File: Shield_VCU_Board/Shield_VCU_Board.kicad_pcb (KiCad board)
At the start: 2 copper layers, 250.5 x 107.1 mm, 156 parts, among them J1 Conn_02x08_Odd_Even, J10 Main_Supply, J11 Conn_01x40_Socket, J13 Conn_Molex_TouchPanel, J14 CAN_OUT, J15 Conn_01x04_Socket, J2 Conn_02x10_Odd_Even, J3/1 NXP3, J4 Conn_02x08_Odd_Even, J5 Conn_02x10_Odd_Even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

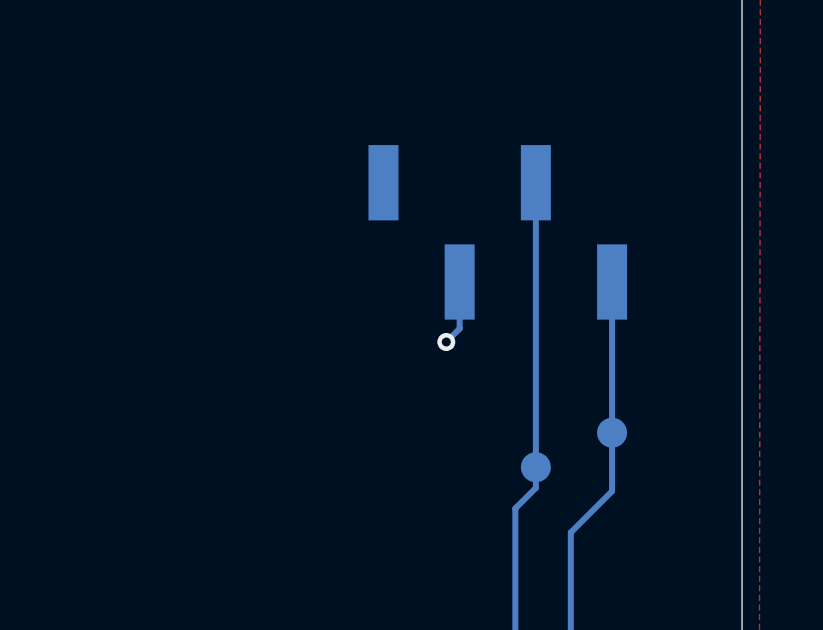
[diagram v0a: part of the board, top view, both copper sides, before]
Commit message: CAN GND removed
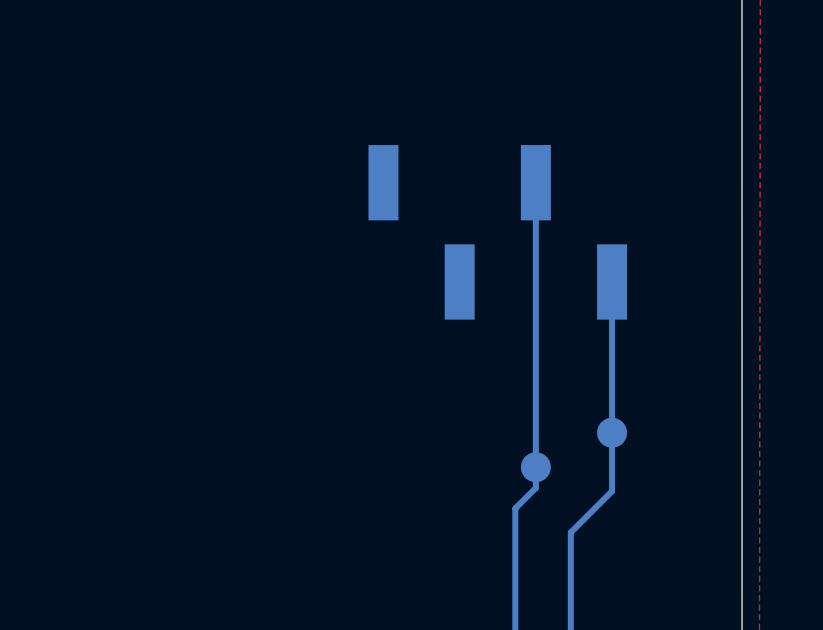
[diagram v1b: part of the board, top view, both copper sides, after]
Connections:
- J15 pad 3: GND -> unconnected-(J15-Pin_3-Pad3)
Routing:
- net GND: track 794.6 -> 792.4 mm, vias 47 -> 46
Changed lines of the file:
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@@
 	(net 253 "Net-(Q4-E)")
 	(net 254 "Net-(Q4-B)")
+	(net 255 "unconnected-(J15-Pin_3-Pad3)")
 	(footprint "MountingHole:MountingHole_2.7mm_M2.5_Pad"
 		(locked yes)
@@
 			(size 2.51 1)
 			(layers "B.Cu" "B.Mask" "B.Paste")
-			(net 35 "GND")
+			(net 255 "unconnected-(J15-Pin_3-Pad3)")
 			(pinfunction "Pin_3")
-			(pintype "passive")
+			(pintype "passive+no_connect")
 		)
 		(pad "4" smd rect
@@
 	)
 	(via
-		(at 265.65 114.65)
-		(size 0.6)
-		(drill 0.3)
-		(layers "F.Cu" "B.Cu")
-		(net 35)
-	)
-	(via
 		(at 178.39 101.98)
 		(size 0.6)
@@
 	)
 	(segment
-		(start 265.65 114.65)
-		(end 266.095 114.205)
-		(width 0.2)
-		(layer "B.Cu")
-		(net 35)
-	)
-	(segment
 		(start 131.7973 75.555878)
 		(end 133.155878 75.555878)
@@
 		(width 0.2)
 		(layer "B.Cu")
-		(net 35)
-	)
-	(segment
-		(start 266.095 114.205)
-		(end 266.095 112.65)
-		(width 0.2)
-		(layer "B.Cu")

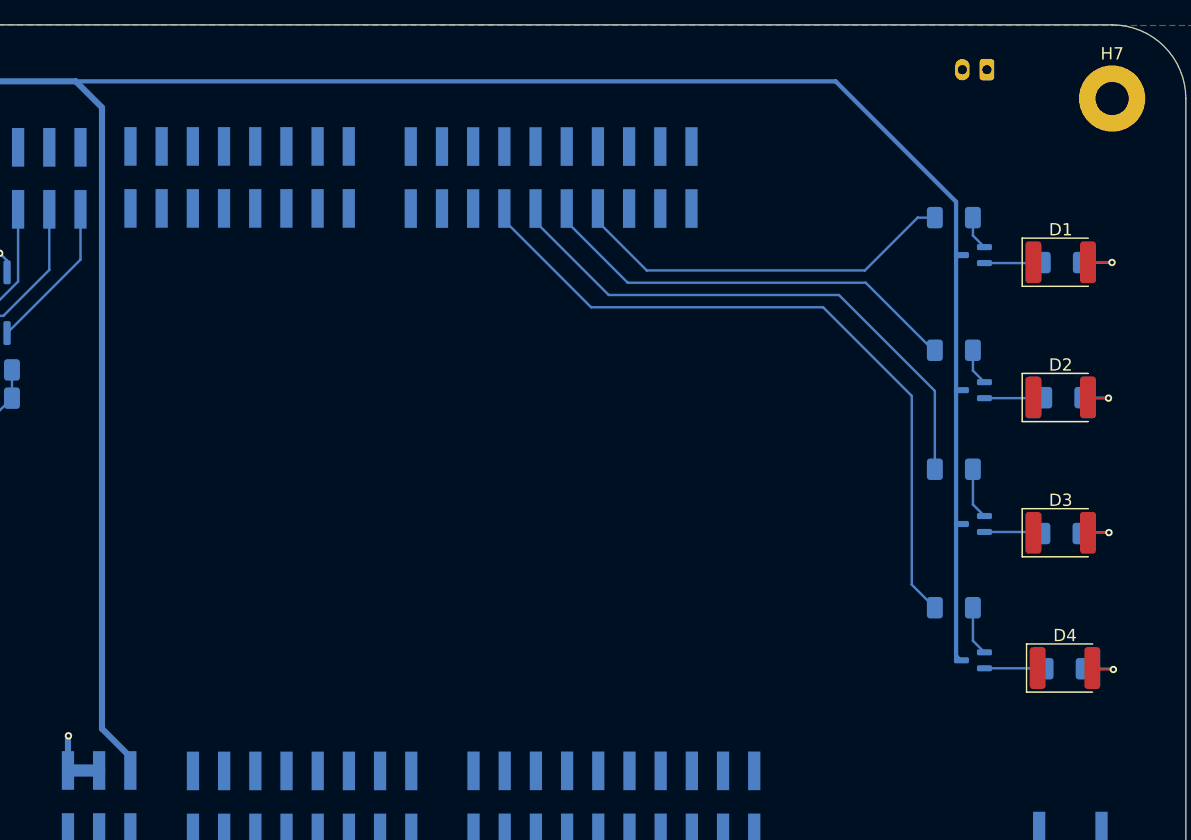
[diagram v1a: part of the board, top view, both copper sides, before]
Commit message: BJT to MOS transfer + new LED
NMOS Datasheet: https://www.onsemi.com/pdf/datasheet/bss138-d.pdf

LED Datasheet:    https://www.mouser.com/catalog/specsheets/ams%20OSRAM_04-30-2025_LS%20ETSF.01_EN.pdf?_gl=1*1llmkcu*_gcl_aw*R0NMLjE3NzI3MDEzNDUuQ2owS0NRandyczJYQmhEakFSSXNBSFZ5bW1UcjlpUWl6aF9Xd1RWYXh4LTl0ajlzSlFKZG9HR05zd3FjQVM0alhPYTRFS0o3bm1nUzBiZ2FBcThfRUFMd193Y0I.*_gcl_au*MTE2NzkxNzkuMTc3MjcwMTMwNy4xMzk2Njg4ODk2LjE3NzQzNTc3NjAuMTc3NDM1Nzc2NA..*_ga*NjEyNjEzMjQ1LjE3NzI3MDEzMDc.*_ga_15W4STQT4T*czE3NzQzNTMzOTckbzE2JGcxJHQxNzc0MzU4MTE2JGoyOCRsMCRoMA..
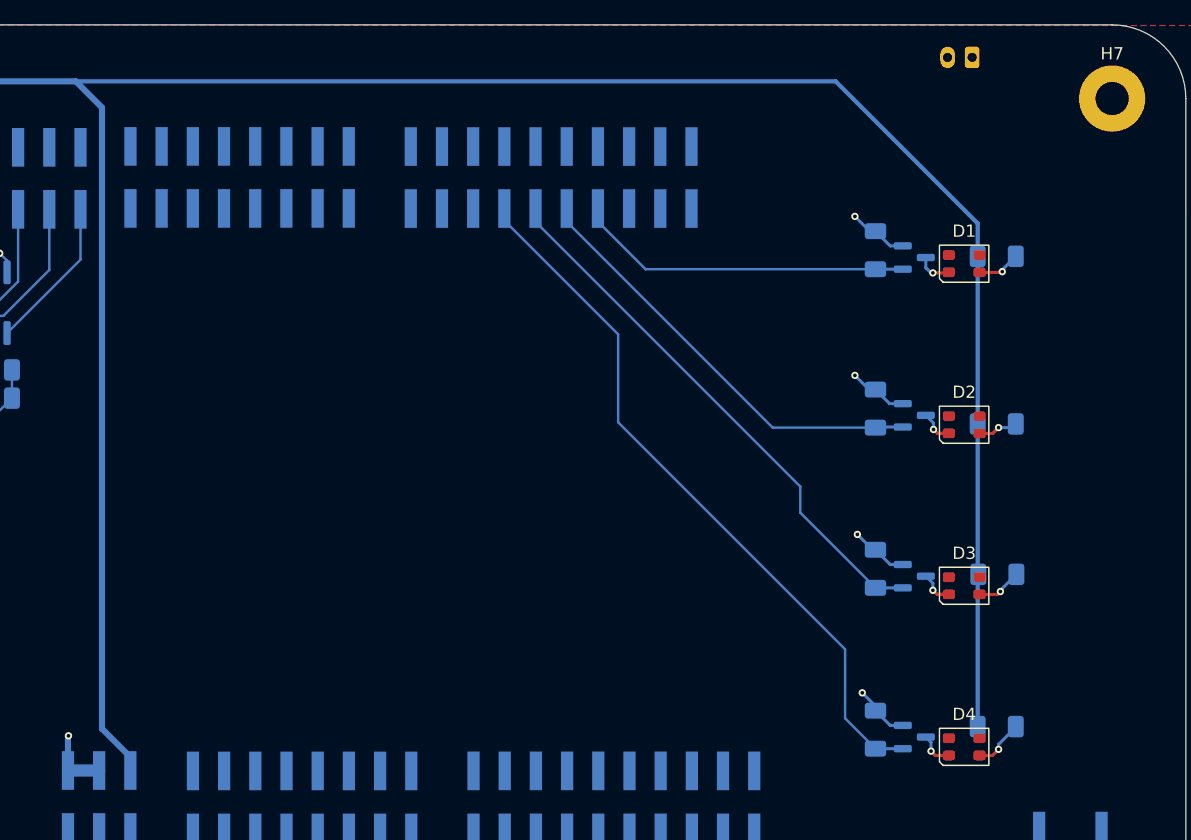
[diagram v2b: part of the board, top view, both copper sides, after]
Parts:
- D1, D2, D3, D4: footprint LED_SMD:LED_1812_4532Metric_Pad1.30x3.40mm_HandSolder -> ALibrary:LED_Cree-PLCC4_3.2x2.8mm_CCW_Corrected
- Q1, Q2, Q3, Q4: value BFR92 -> BSS138; footprint Package_TO_SOT_SMD:SOT-323_SC-70 -> Package_TO_SOT_SMD:SOT-23
- R1, R17, R18, R23: value 1k -> 1M
- R2, R3, R4, R5: value 1k -> 220R
- moved R23 11.8 mm to (250.2, 101.4), turned to -90 degrees
- moved D4 10.4 mm to (257.4, 102.8)
- moved R18 10.3 mm to (250.2, 88.3), turned to -90 degrees
- moved D3 8.97 mm to (257.4, 89.7)
- moved D2 8.17 mm to (257.4, 76.6)
- moved R17 7.96 mm to (250.2, 75.2), turned to -90 degrees
- moved Q4 7.87 mm to (253.4, 102.0), turned to 0 degrees
- moved D1 7.86 mm to (257.4, 63.5)
- moved R5 7.26 mm to (260.1, 101.2)
- moved R1 6.91 mm to (250.2, 62.3), turned to -90 degrees
- moved Q3 6.39 mm to (253.4, 88.9), turned to 0 degrees
- moved R4 6.19 mm to (260.1, 88.8)
- moved R3 5.83 mm to (260.1, 76.5)
- moved R2 5.32 mm to (260.1, 62.9)
- moved Q2 5.20 mm to (253.4, 75.8), turned to 0 degrees
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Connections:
- D1 pad 1: GND -> Net-(D1-K)
- D2 pad 1: GND -> Net-(D2-K)
- D3 pad 1: GND -> Net-(D3-K)
- D4 pad 1: GND -> Net-(D4-K)
- Q1 pad 1: Net-(Q1-B) -> LED1_PTB9
- Q1 pad 2: Net-(Q1-E) -> GND
- Q1 pad 3: +12V -> Net-(D1-K)
- Q2 pad 1: Net-(Q2-B) -> LED2_PTA12
- Q2 pad 2: Net-(Q2-E) -> GND
- Q2 pad 3: +12V -> Net-(D2-K)
- Q3 pad 1: Net-(Q3-B) -> LED3_PTA24
- Q3 pad 2: Net-(Q3-E) -> GND
- Q3 pad 3: +12V -> Net-(D3-K)
- Q4 pad 1: Net-(Q4-B) -> LED4_PTA25
- Q4 pad 2: Net-(Q4-E) -> GND
- Q4 pad 3: +12V -> Net-(D4-K)
- R1 pad 1: LED1_PTB9 -> GND
- R1 pad 2: Net-(Q1-B) -> LED1_PTB9
- R17 pad 1: LED2_PTA12 -> GND
- R17 pad 2: Net-(Q2-B) -> LED2_PTA12
- R18 pad 1: LED3_PTA24 -> GND
- R18 pad 2: Net-(Q3-B) -> LED3_PTA24
- R2 pad 1: Net-(Q1-E) -> +12V
- R23 pad 1: LED4_PTA25 -> GND
- R23 pad 2: Net-(Q4-B) -> LED4_PTA25
- R3 pad 1: Net-(Q2-E) -> +12V
- R4 pad 1: Net-(Q3-E) -> +12V
- R5 pad 1: Net-(Q4-E) -> +12V
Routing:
- net GND: track 792.4 -> 811.5 mm, vias 46 -> 50
- net +12V: track 458.7 -> 464.5 mm
- net Net-(Q4-E): track 5.00 -> 0.00 mm
- net Net-(Q2-E): track 4.89 -> 0.00 mm
- net Net-(Q3-E): track 4.77 -> 0.00 mm
- net Net-(Q1-E): track 4.77 -> 0.00 mm
- net LED1_PTB9: track 31.9 -> 27.5 mm
- net Net-(Q3-B): track 4.20 -> 0.00 mm
- net Net-(Q4-B): track 4.02 -> 0.00 mm
- net Net-(Q2-B): track 2.99 -> 0.00 mm
- net Net-(D4-K): track 0.00 -> 2.92 mm, vias 0 -> 1
- net Net-(D1-K): track 0.00 -> 2.90 mm, vias 0 -> 1
- net Net-(D3-K): track 0.00 -> 2.83 mm, vias 0 -> 1
- net Net-(D2-K): track 0.00 -> 2.79 mm, vias 0 -> 1
- net Net-(Q1-B): track 2.79 -> 0.00 mm
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
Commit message: New Pin assignment
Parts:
- moved J7 86.8 mm to (269.8, 132.7)
- moved J14 2.05 mm to (269.8, 124.8), turned to 180 degrees
- moved R3 1.52 mm to (259.1, 75.3)
- moved R5 1.32 mm to (258.8, 101.4)
- moved R4 1.15 mm to (259.0, 88.8)
- moved R2 1.11 mm to (259.0, 62.7)
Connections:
- CAN_H1 pad 1: Net-(J14-Pin_2) -> Net-(J14-Pin_1)
- CAN_L1 pad 1: Net-(J14-Pin_1) -> Net-(J14-Pin_2)
- J15 pad 1: Net-(J14-Pin_2) -> Net-(J14-Pin_1)
- J15 pad 2: Net-(J14-Pin_1) -> Net-(J14-Pin_2)
- J2 pad 12: Net-(J2-Pin_12) -> unconnected-(J2-Pin_12-Pad12)
- J2 pad 15: AUD_SHDN -> unconnected-(J2-Pin_15-Pad15)
- J2 pad 16: unconnected-(J2-Pin_16-Pad16) -> AUD_SHDN
- J2 pad 18: Net-(J2-Pin_18) -> unconnected-(J2-Pin_18-Pad18)
- J3/1 pad 1: GND -> unconnected-(J3/1-Pin_1-Pad1)
- J5 pad 18: unconnected-(J5-Pin_18-Pad18) -> Net-(J5-Pin_18)
- J5 pad 20: unconnected-(J5-Pin_20-Pad20) -> Net-(J5-Pin_20)
- J7 pad 1: Net-(J2-Pin_18) -> Net-(J5-Pin_20)
- J7 pad 2: Net-(J2-Pin_12) -> Net-(J5-Pin_18)
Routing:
- net Net-(J5-Pin_18): track 0.00 -> 40.1 mm
- net Net-(J5-Pin_20): track 0.00 -> 39.5 mm
- net AUD_SHDN: track 91.0 -> 95.8 mm
- net Net-(J14-Pin_1): track 16.2 -> 12.7 mm
- net Net-(J14-Pin_2): track 13.1 -> 15.8 mm
- net GND: track 811.5 -> 809.2 mm
- net unconnected-(J2-Pin_15-Pad15): track 0.00 -> 1.16 mm
- net Net-(D4-A): track 4.21 -> 3.40 mm
- net Net-(D3-A): track 3.74 -> 3.16 mm

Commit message: NMOS correction
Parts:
- moved R23 5.80 mm to (253.7, 96.8), turned to 180 degrees
- moved R17 5.52 mm to (254.1, 71.3), turned to 180 degrees
- moved R18 5.06 mm to (253.9, 84.8), turned to 180 degrees
- moved Q4 2.05 mm to (253.1, 100.0), turned to -90 degrees
- moved Q1 1.98 mm to (251.8, 64.2)
- moved R1 1.98 mm to (248.6, 63.5)
- moved Q2 1.37 mm to (253.5, 74.4), turned to -90 degrees
- moved Q3 0.92 mm to (253.3, 88.0), turned to -90 degrees
- moved R5 0.25 mm to (259.1, 101.5)
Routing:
- net LED4_PTA25: track 58.7 -> 53.7 mm
- net Net-(D4-K): track 2.92 -> 4.71 mm
- net Net-(7U1-G): track 167.3 -> 165.7 mm
- net Net-(7U1-B): track 166.4 -> 164.9 mm
- net Net-(7U1-F): track 160.4 -> 159.1 mm
- net LED1_PTB9: track 27.5 -> 26.4 mm
- net Net-(D2-K): track 2.79 -> 3.73 mm
- net Net-(D3-K): track 2.83 -> 3.75 mm
- net LED3_PTA24: track 44.6 -> 43.7 mm
- net GND: track 809.2 -> 808.3 mm
- net Net-(D1-K): track 2.90 -> 3.49 mm
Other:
- board text added: "Here could be your Logo ! But you have no money..."

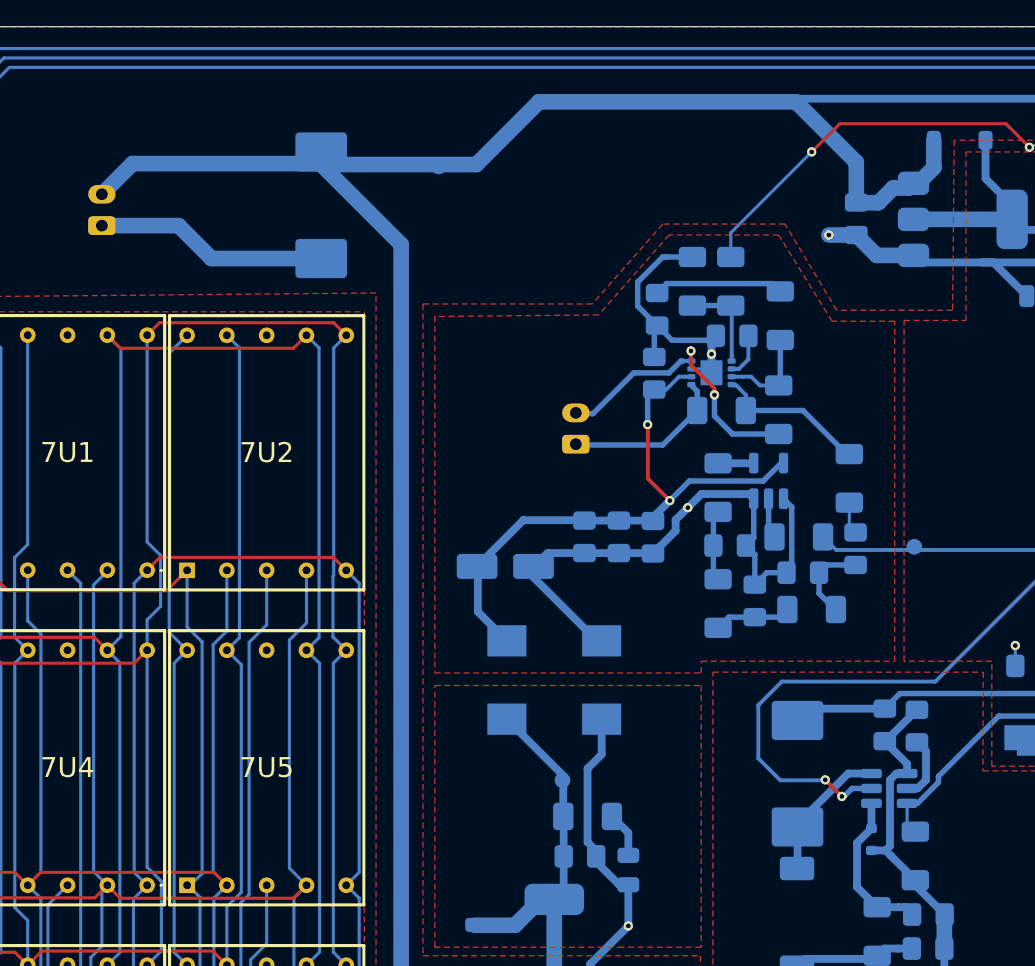
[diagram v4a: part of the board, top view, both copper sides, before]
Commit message: SHOTTKY x2 size change
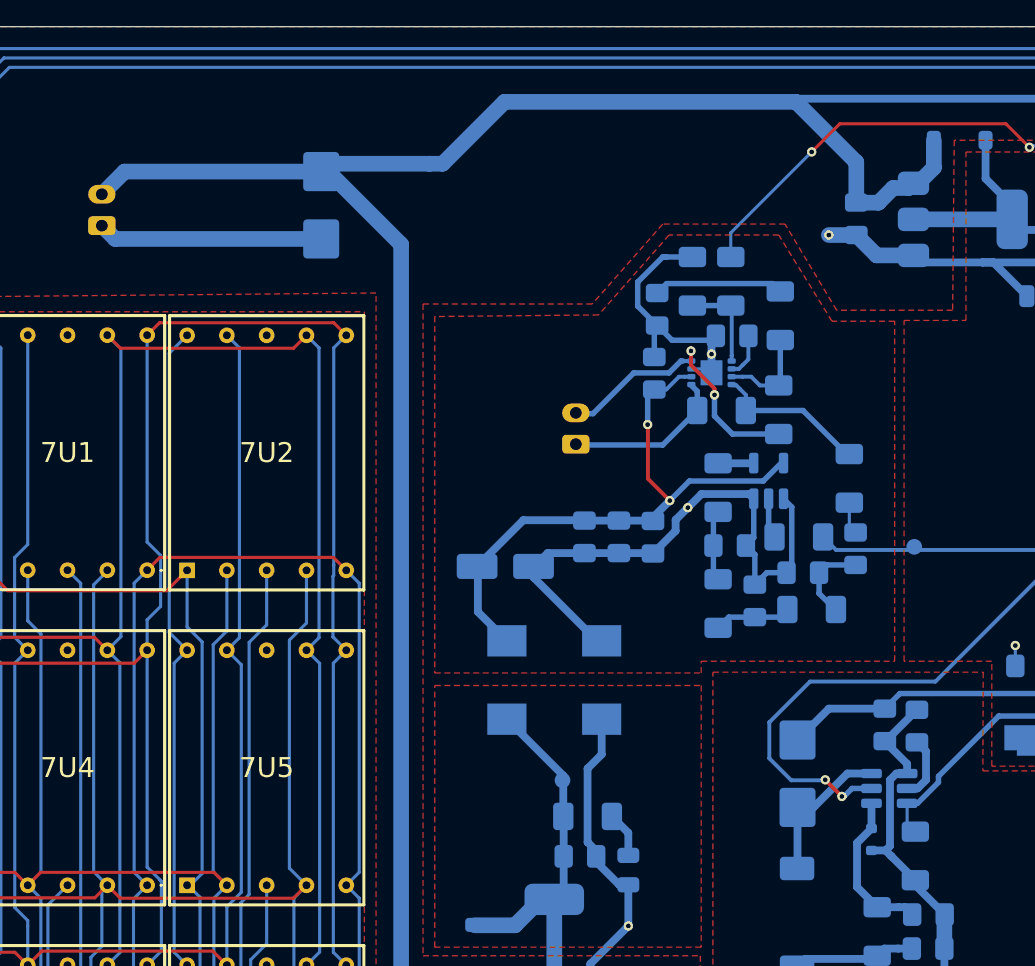
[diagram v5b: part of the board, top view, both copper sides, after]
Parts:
- D15, D16: footprint Diode_SMD:D_SMC -> Diode_SMD:D_SMB
- moved V12 0.62 mm to (68.9, 52.8)
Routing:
- net BL_PWM: track 55.4 -> 53.4 mm
- net Net-(D16-A): track 8.90 -> 10.6 mm
- net GND: track 808.3 -> 807.4 mm

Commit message: Logos_Added
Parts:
- added G***: LOGO, LOGO, F.Cu at (53.7, 143.4)
- added G***: LOGO, LOGO, F.Cu at (54.9, 47.5)
- D1, D2, D3, D4: footprint ALibrary:LED_Cree-PLCC4_3.2x2.8mm_CCW_Corrected -> ALibrary:LED_Cree-PLCC4_3.2x2.8mm_CCW_Orange
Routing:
- net Net-(D1-A): track 3.07 -> 1.62 mm
- net Net-(D1-K): track 3.49 -> 2.24 mm
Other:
- board text removed: "Here could be your Logo ! But you have no money..."

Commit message: Gerber_files_created_V1.0
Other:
- board text removed: "MOTHERBOARD (250X107)"
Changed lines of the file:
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@@
 			(outputformat 1)
 			(mirror no)
-			(drillshape 1)
+			(drillshape 0)
 			(scaleselection 1)
-			(outputdirectory "")
+			(outputdirectory "Gerbers/")
 		)
 	)
@@
 			(at 0 3.65 0)
 			(layer "F.Fab")
+			(hide yes)
 			(effects
 				(font
@@
 			(at -4.1 3.9 0)
 			(layer "F.Fab")
+			(hide yes)
 			(effects
 				(font
@@
 			(at 0 3.65 0)
 			(layer "F.Fab")
+			(hide yes)
 			(effects
 				(font
@@
 			(at 0 3.65 0)
 			(layer "F.Fab")
+			(hide yes)
 			(effects
 				(font
@@
 		)
 		(property "Value" "Button_Activation_Logic"
-			(at 1 -4 0)
+			(at 4.95 -4.4 0)
 			(layer "B.Fab")
 			(effects
@@
 		)
 	)
-	(gr_text "MOTHERBOARD (250X107)"
-		(at 140.3 39.95 0)
-		(layer "F.Paste")
-		(effects
-			(font
-				(size 6 6)
-				(thickness 1.2)
-				(bold yes)
-			)
-			(justify left bottom)
-		)
-	)
 	(gr_text "L2"
 		(locked yes)
@@
 		)
 	)
-	(dimension
-		(type orthogonal)
-		(layer "F.Paste")
-		(pts
-			(xy 31 44) (xy 31 151.1)
-		)
-		(height -10.7)
-		(orientation 1)
-		(format
-			(prefix "")
-			(suffix "")
-			(units 3)
-			(units_format 0)
-			(precision 4)
-			(suppress_zeroes yes)
-		)
-		(style
-			(thickness 0.1)
-			(arrow_length 1.27)
-			(text_position_mode 0)
-			(arrow_direction outward)
-			(extension_height 0.58642)
-			(extension_offset 0.5)
-			(keep_text_aligned yes)
-		)
-		(gr_text "107.1"
-			(at 19.15 97.55 90)
-			(layer "F.Paste")
-			(effects
-				(font
-					(size 1 1)
-					(thickness 0.15)
-				)
-			)
-		)
-	)
-	(dimension
-		(type orthogonal)
-		(locked yes)
-		(layer "F.Paste")
-		(pts
-			(xy 182.1 149.2) (xy 104.55 149.2)
-		)
-		(height 6.35)
-		(orientation 0)
-		(format
-			(prefix "")
-			(suffix "")
-			(units 3)
-			(units_format 0)
-			(precision 4)
-			(suppress_zeroes yes)
-		)
-		(style
-			(thickness 0.1)
-			(arrow_length 1.27)
-			(text_position_mode 0)
-			(arrow_direction outward)
-			(extension_height 0.58642)
-			(extension_offset 0.5)
-			(keep_text_aligned yes)
-		)
-		(gr_text "77.55"
-			(locked yes)
-			(at 143.325 154.4 0)
-			(layer "F.Paste")
-			(effects
-				(font
-					(size 1 1)
-					(thickness 0.15)
-				)
-			)
-		)
-	)
-	(dimension
-		(type orthogonal)
-		(locked yes)
-		(layer "F.Paste")
-		(pts
-			(xy 184 151.1) (xy 179.7 124.61)
-		)
-		(height -9.7)
-		(orientation 1)
-		(format
-			(prefix "")
-			(suffix "")
-			(units 3)
-			(units_format 0)
-			(precision 4)
-			(suppress_zeroes yes)
-		)
-		(style
-			(thickness 0.1)
-			(arrow_length 1.27)
-			(text_position_mode 0)
-			(arrow_direction outward)
-			(extension_height 0.58642)
-			(extension_offset 0.5)
-			(keep_text_aligned yes)
-		)
-		(gr_text "26.49"
-			(locked yes)
-			(at 173.15 137.855 90)
-			(layer "F.Paste")
-			(effects
-				(font
-					(size 1 1)
-					(thickness 0.15)
-				)
-			)
-		)
-	)
-	(dimension
-		(type orthogonal)
-		(locked yes)
-		(layer "F.Paste")
-		(pts
-			(xy 275.5 140.1) (xy 25.1 140.2)
-		)
-		(height 20.59)
-		(orientation 0)
-		(format
-			(prefix "")
-			(suffix "")
-			(units 3)
-			(units_format 0)
-			(precision 4)
-			(suppress_zeroes yes)
-		)
-		(style
-			(thickness 0.2)
-			(arrow_length 1.27)
-			(text_position_mode 0)
-			(arrow_direction outward)
-			(extension_height 0.58642)
-			(extension_offset 0.5)
-			(keep_text_aligned yes)
-		)
-		(gr_text "250.4"
-			(locked yes)
-			(at 150.3 158.89 0)
-			(layer "F.Paste")
-			(effects
-				(font
-					(size 1.5 1.5)
-					(thickness 0.3)
-				)
-			)
-		)
-	)

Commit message: Gerber_settings_changed
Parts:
- moved G*** 1.84 mm to (53.7, 141.5)
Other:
- board text added: "25 Mar 2026 - v1.0"
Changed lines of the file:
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@@
 			(plot_on_all_layers_selection 0x00000000_00000000_00000000_00000000)
 			(disableapertmacros no)
-			(usegerberextensions no)
-			(usegerberattributes yes)
-			(usegerberadvancedattributes yes)
-			(creategerberjobfile yes)
+			(usegerberextensions yes)
+			(usegerberattributes no)
+			(usegerberadvancedattributes no)
+			(creategerberjobfile no)
 			(dashed_line_dash_ratio 12.000000)
 			(dashed_line_gap_ratio 3.000000)
@@
 	)
 	(footprint "LOGO"
-		(locked yes)
 		(layer "F.Cu")
-		(at 53.742356 143.373154)
+		(at 53.66591 141.53075)
 		(property "Reference" "G***"
 			(at 0 0 0)
@@
 	)
 	(footprint "LOGO"
-		(locked yes)
 		(layer "F.Cu")
 		(at 54.920635 47.503932)
@@
 		(layer "Edge.Cuts")
 	)
+	(gr_text "25 Mar 2026 - v1.0"
+		(at 50.41 149.67 0)
+		(layer "F.SilkS")
+		(effects
+			(font
+				(size 1 1)
+				(thickness 0.2)
+				(bold yes)
+			)
+			(justify left bottom)
+		)
+	)
 	(gr_text "Display\n"
 		(locked yes)
@@
 	)
 	(group ""
-		(locked yes)
-		(members "3249af7d-2f40-4784-a4e9-71d1209a8715" "8a2878dd-4f9a-460e-951d-db4c7e8b7da0")
-	)
-	(group ""
